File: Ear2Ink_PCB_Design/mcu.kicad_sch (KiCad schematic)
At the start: 11 parts, among them U1 STM32F411RETx

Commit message: added some stuff
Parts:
- added C14: 0.1uF, symbol Device:C
- added C15: 200pF, symbol Device:C
- added J1: Conn_02x16_Top_Bottom, symbol Connector_Generic:Conn_02x16_Top_Bottom
- added MK1: SPH0645LM4H, Sensor_Audio:Knowles_SPH0645LM4H-6_3.5x2.65mm, symbol Sensor_Audio:SPH0645LM4H
- added R3: R_US, symbol Device:R_US
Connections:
- net +3.3V: now also C14.1, C15.1, MK1.2 (SEL), MK1.5 (VDD)
- net GND: now also C14.2, C15.2, MK1.3 (GND)
- net I2S2_SD: now reaches U1.11 (PC3)
- net I2S2_SD: now also R3.1
- net I2S2_MCK: now reaches U1.22 (PA6)
- net I2S2_CK: now reaches U1.29 (PB10)
- net I2S2_CK: now also MK1.4 (BCLK)
- net I2S2_WS: now reaches U1.33 (PB12)
- net I2S2_WS: now also MK1.1 (WS)
- new net: MK1.6 (DATA), R3.2
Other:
- note added: "Note: add or remove these based on trace length"

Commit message: added osc
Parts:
- added C18: 0.1uF, symbol Device:C
- added Y1: MAX7375AXR805, Package_TO_SOT_SMD:SOT-323_SC-70, symbol Oscillator:MAX7375AXR805
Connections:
- net +3.3V: now also J1.18 (Pin_18), J1.2 (Pin_2), C18.1, Y1.1 (V+)
- net GND: now also J1.1 (Pin_1), J1.17 (Pin_17), C18.2, Y1.3 (GND)
- new net RCC_OSC_IN: Y1.2 (CLOCK)

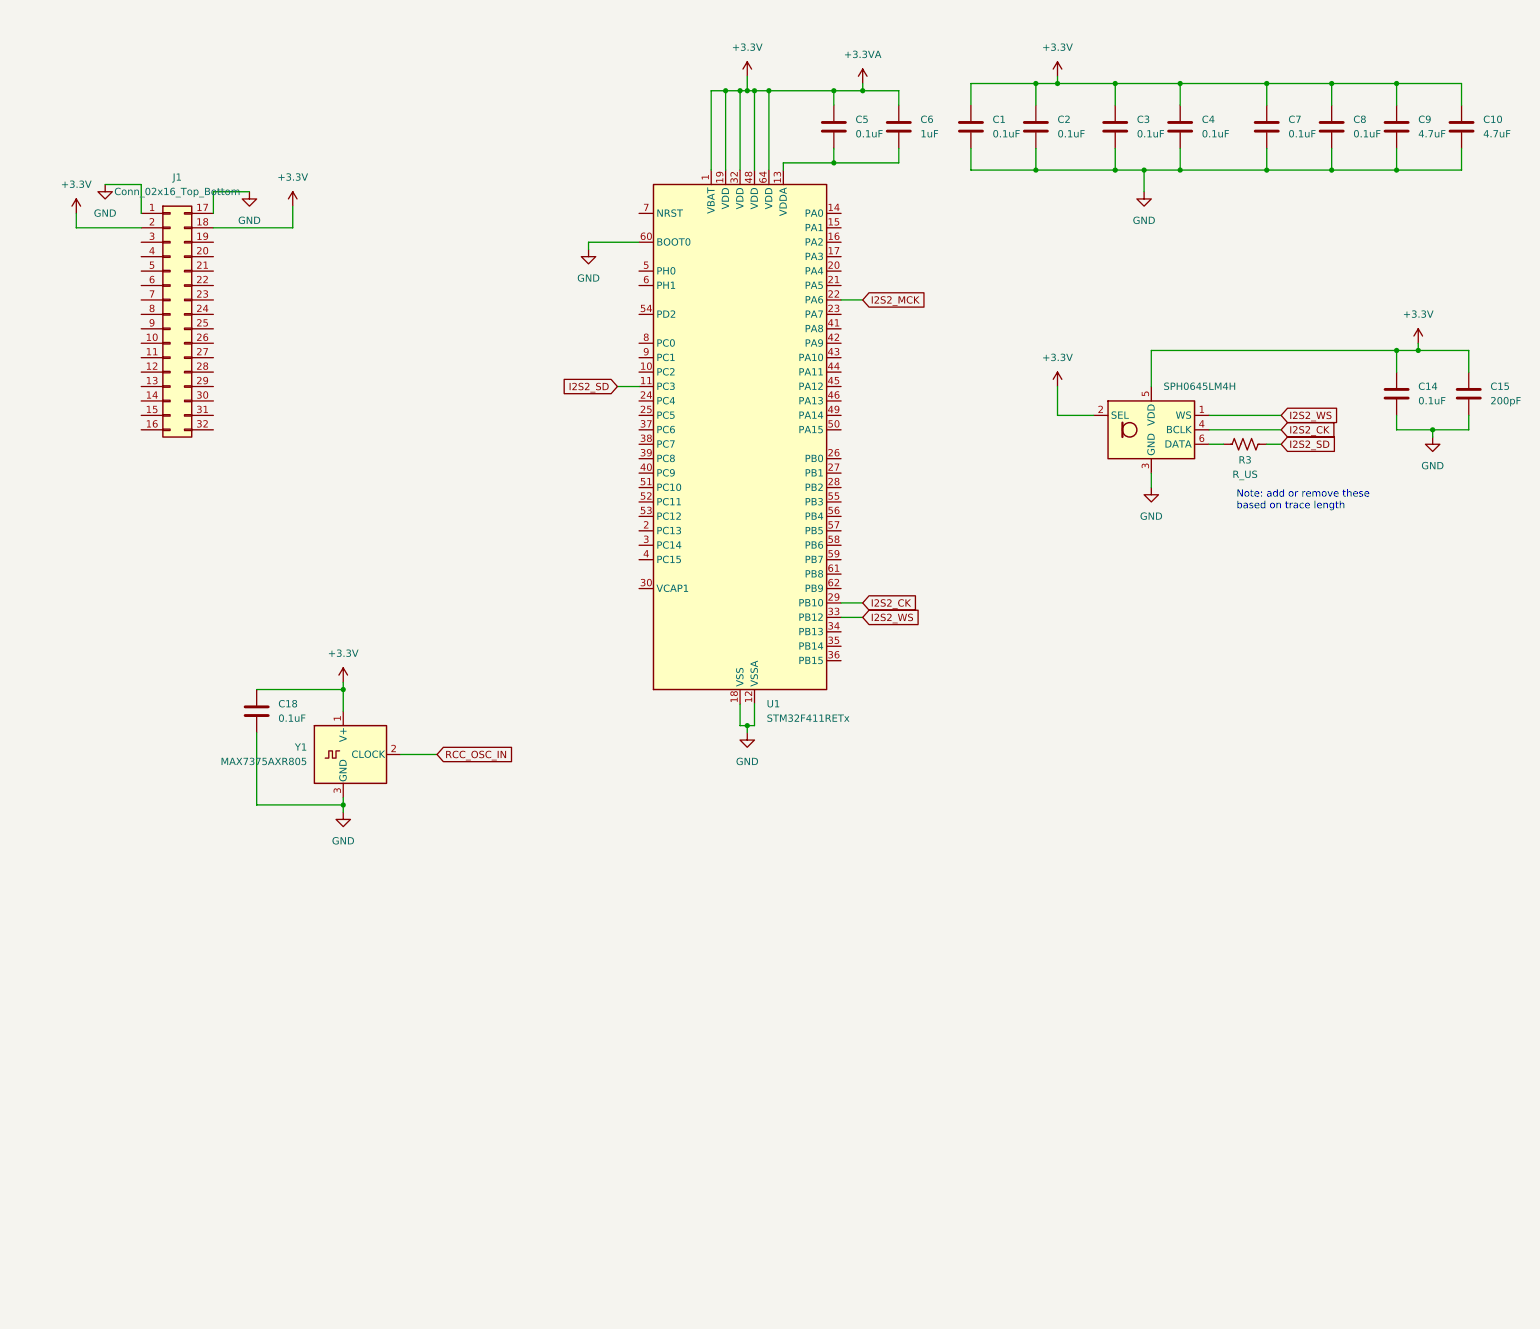
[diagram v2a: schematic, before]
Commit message: wired LCD and keypad
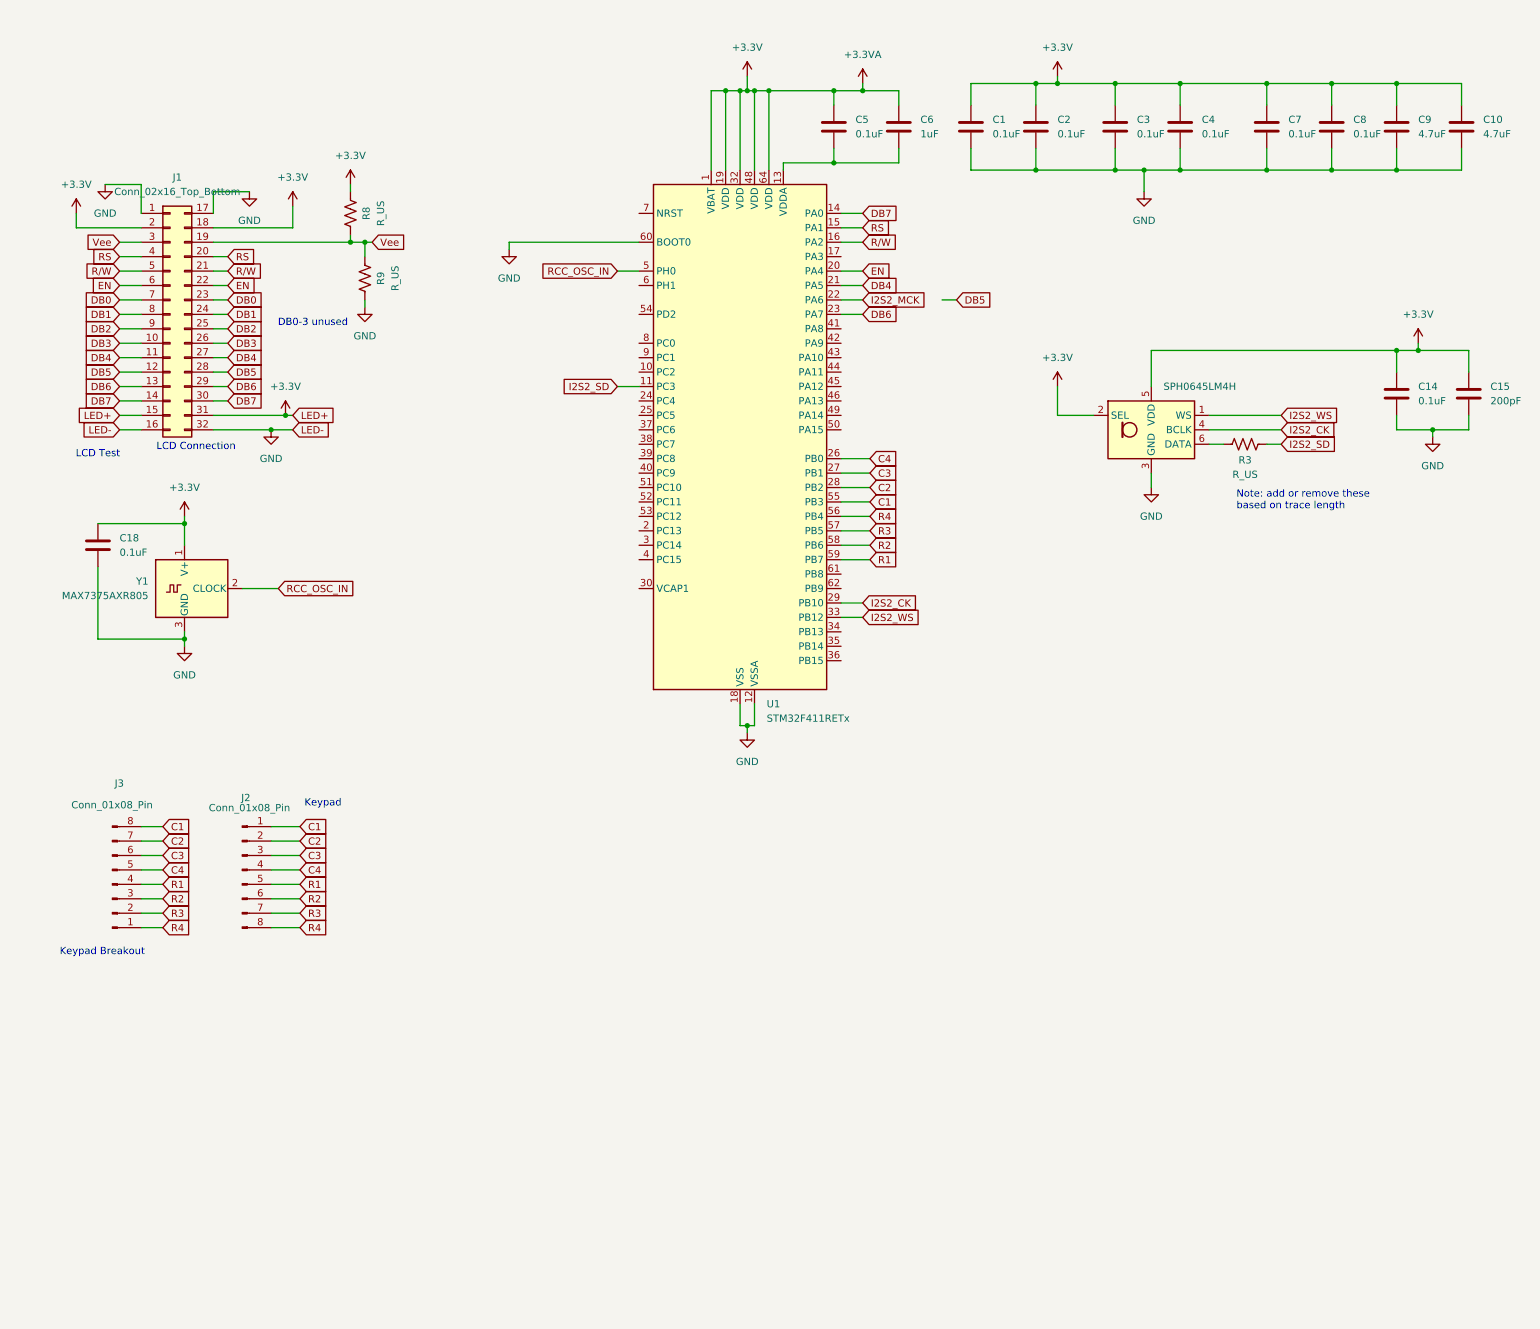
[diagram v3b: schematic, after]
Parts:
- added J2, J3: Conn_01x08_Pin, symbol Connector:Conn_01x08_Pin
- added R8, R9: R_US, symbol Device:R_US
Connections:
- net +3.3V: now also J1.15 (Pin_15), J1.31 (Pin_31), R8.1
- net GND: now also J1.16 (Pin_16), J1.32 (Pin_32), R9.2
- net RCC_OSC_IN: now also U1.5 (PH0)
- net DB7: now reaches U1.14 (PA0)
- net DB7: now also J1.14 (Pin_14), J1.30 (Pin_30)
- net RS: now reaches U1.15 (PA1)
- net RS: now also J1.20 (Pin_20), J1.4 (Pin_4)
- net R/W: now reaches U1.16 (PA2)
- net R/W: now also J1.21 (Pin_21), J1.5 (Pin_5)
- net EN: now reaches U1.20 (PA4)
- net EN: now also J1.22 (Pin_22), J1.6 (Pin_6)
- net DB4: now reaches U1.21 (PA5)
- net DB4: now also J1.11 (Pin_11), J1.27 (Pin_27)
- net DB6: now reaches U1.23 (PA7)
- net DB6: now also J1.13 (Pin_13), J1.29 (Pin_29)
- net C4: now reaches U1.26 (PB0)
- net C4: now also J2.4 (Pin_4), J3.5 (Pin_5)
- net C3: now reaches U1.27 (PB1)
- net C3: now also J2.3 (Pin_3), J3.6 (Pin_6)
- net C2: now reaches U1.28 (PB2)
- net C2: now also J2.2 (Pin_2), J3.7 (Pin_7)
- net C1: now reaches U1.55 (PB3)
- net C1: now also J2.1 (Pin_1), J3.8 (Pin_8)
- net R4: now reaches U1.56 (PB4)
- net R4: now also J2.8 (Pin_8), J3.1 (Pin_1)
- net R3: now reaches U1.57 (PB5)
- net R3: now also J2.7 (Pin_7), J3.2 (Pin_2)
- net R2: now reaches U1.58 (PB6)
- net R2: now also J2.6 (Pin_6), J3.3 (Pin_3)
- net R1: now reaches U1.59 (PB7)
- net R1: now also J2.5 (Pin_5), J3.4 (Pin_4)
- net DB3: now reaches J1.10 (Pin_10)
- net DB3: now also J1.26 (Pin_26)
- net DB5: now reaches J1.12 (Pin_12)
- net DB5: now also J1.28 (Pin_28)
- net Vee: now reaches J1.19 (Pin_19)
- net Vee: now also J1.3 (Pin_3), R8.2, R9.1
- net DB0: now reaches J1.23 (Pin_23)
- net DB0: now also J1.7 (Pin_7)
- net DB1: now reaches J1.24 (Pin_24)
- net DB1: now also J1.8 (Pin_8)
- net DB2: now reaches J1.25 (Pin_25)
- net DB2: now also J1.9 (Pin_9)
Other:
- note added: "DB0-3 unused"
- note added: "Keypad"
- note added: "Keypad Breakout"
- note added: "LCD Connection"
- note added: "LCD Test"
- moved on the sheet: C18, Y1

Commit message: everything except voltage monitor on schematic
no footprints assigned yet
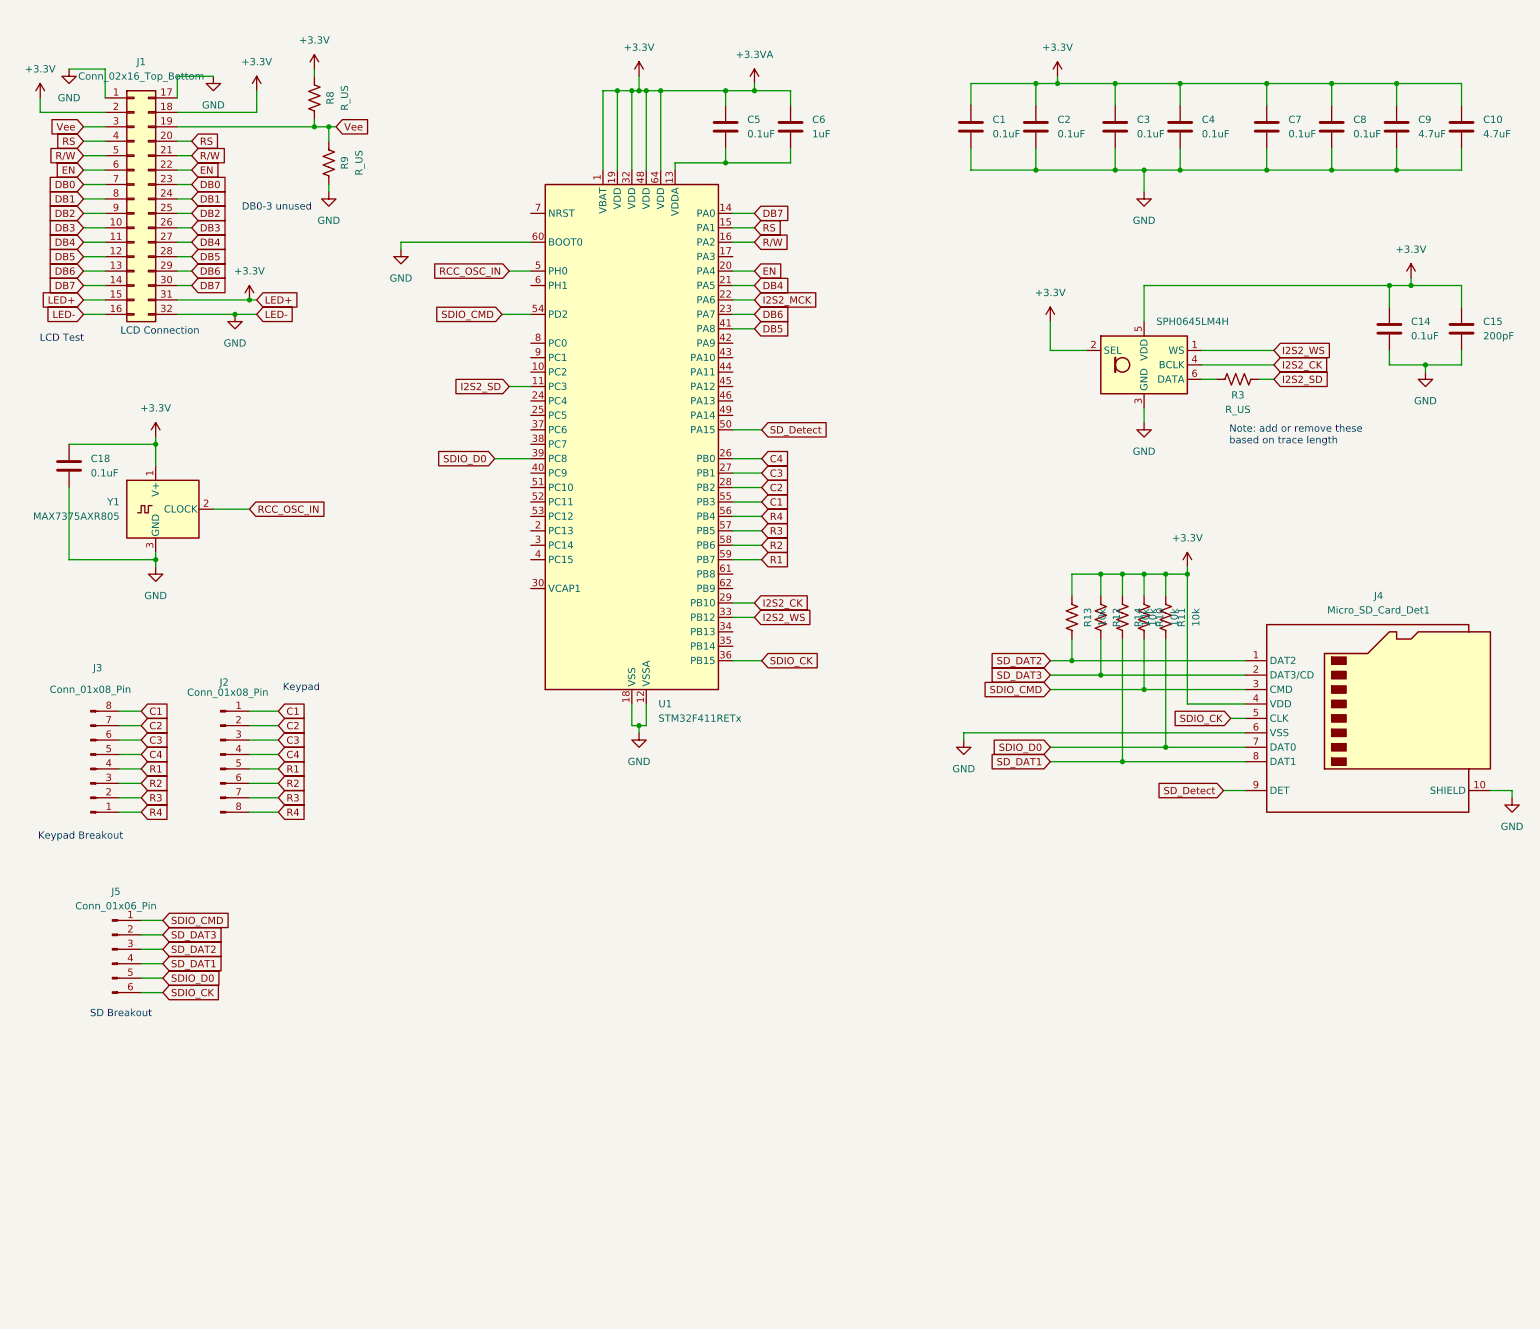
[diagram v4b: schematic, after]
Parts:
- added J4: Micro_SD_Card_Det1, symbol Connector:Micro_SD_Card_Det1
- added J5: Conn_01x06_Pin, symbol Connector:Conn_01x06_Pin
- added R10, R11, R12, R13, R14: 10k, symbol Device:R_US
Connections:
- net +3.3V: now also J4.4 (VDD), R10.1, R11.1, R12.1, R13.1, R14.1
- net DB5: now also U1.41 (PA8)
- net GND: now also J4.10 (SHIELD), J4.6 (VSS)
- net SDIO_CK: now reaches U1.36 (PB15)
- net SDIO_CK: now also J4.5 (CLK), J5.6 (Pin_6)
- net SDIO_D0: now reaches U1.39 (PC8)
- net SDIO_D0: now also J4.7 (DAT0), J5.5 (Pin_5), R11.2
- net SD_Detect: now reaches U1.50 (PA15)
- net SD_Detect: now also J4.9 (DET)
- net SDIO_CMD: now reaches U1.54 (PD2)
- net SDIO_CMD: now also J4.3 (CMD), J5.1 (Pin_1), R10.2
- new net SD_DAT1: J4.8 (DAT1), J5.4 (Pin_4), R14.2
- new net SD_DAT2: J4.1 (DAT2), J5.3 (Pin_3), R13.2
- new net SD_DAT3: J4.2 (DAT3/CD), J5.2 (Pin_2), R12.2
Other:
- note added: "SD Breakout"
- moved on the sheet: C14, C15, C18, C5, C6, J1, J2, J3, R3, R8, R9, U1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

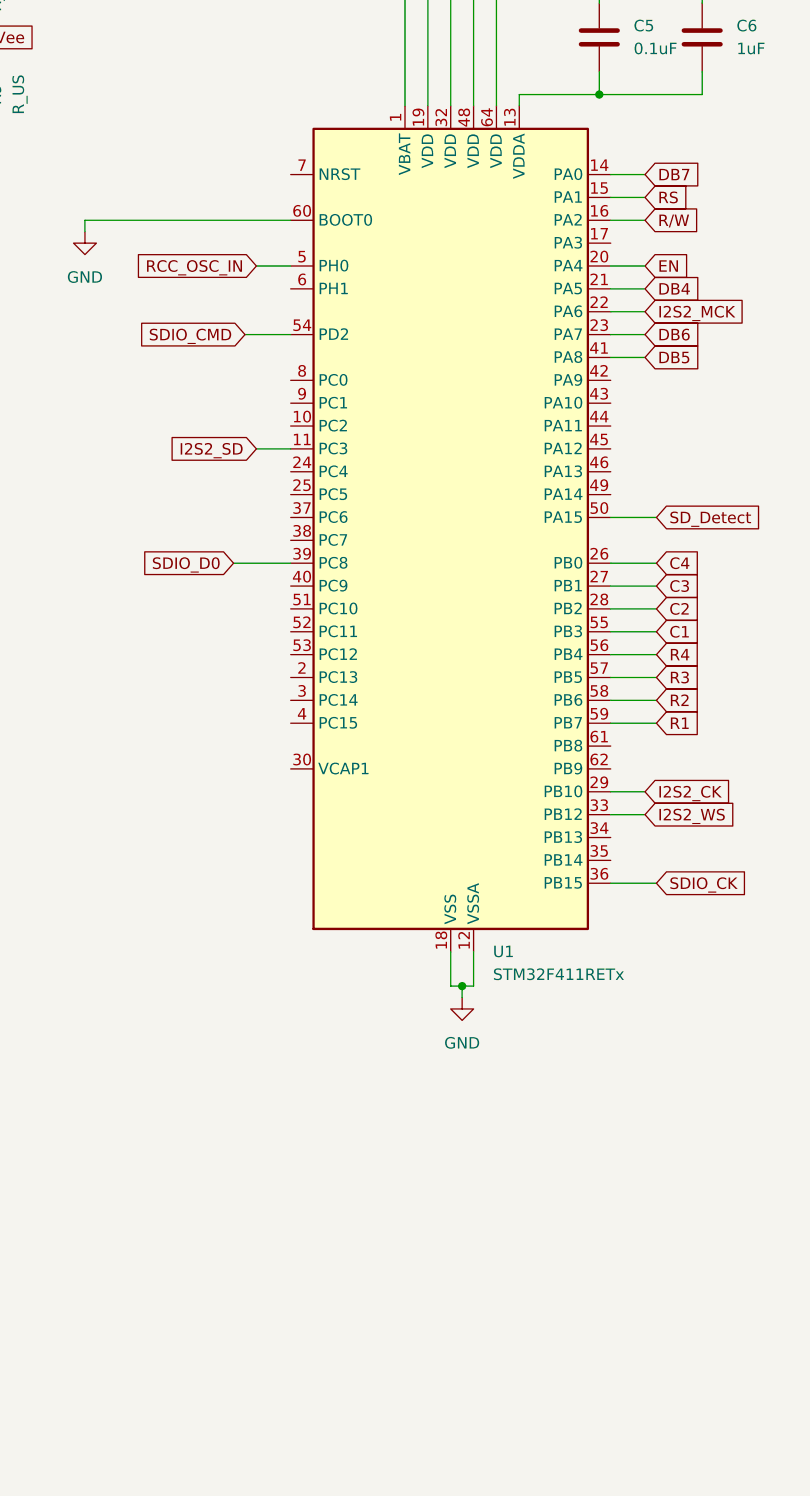
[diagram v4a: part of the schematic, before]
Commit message: started assigning footprints
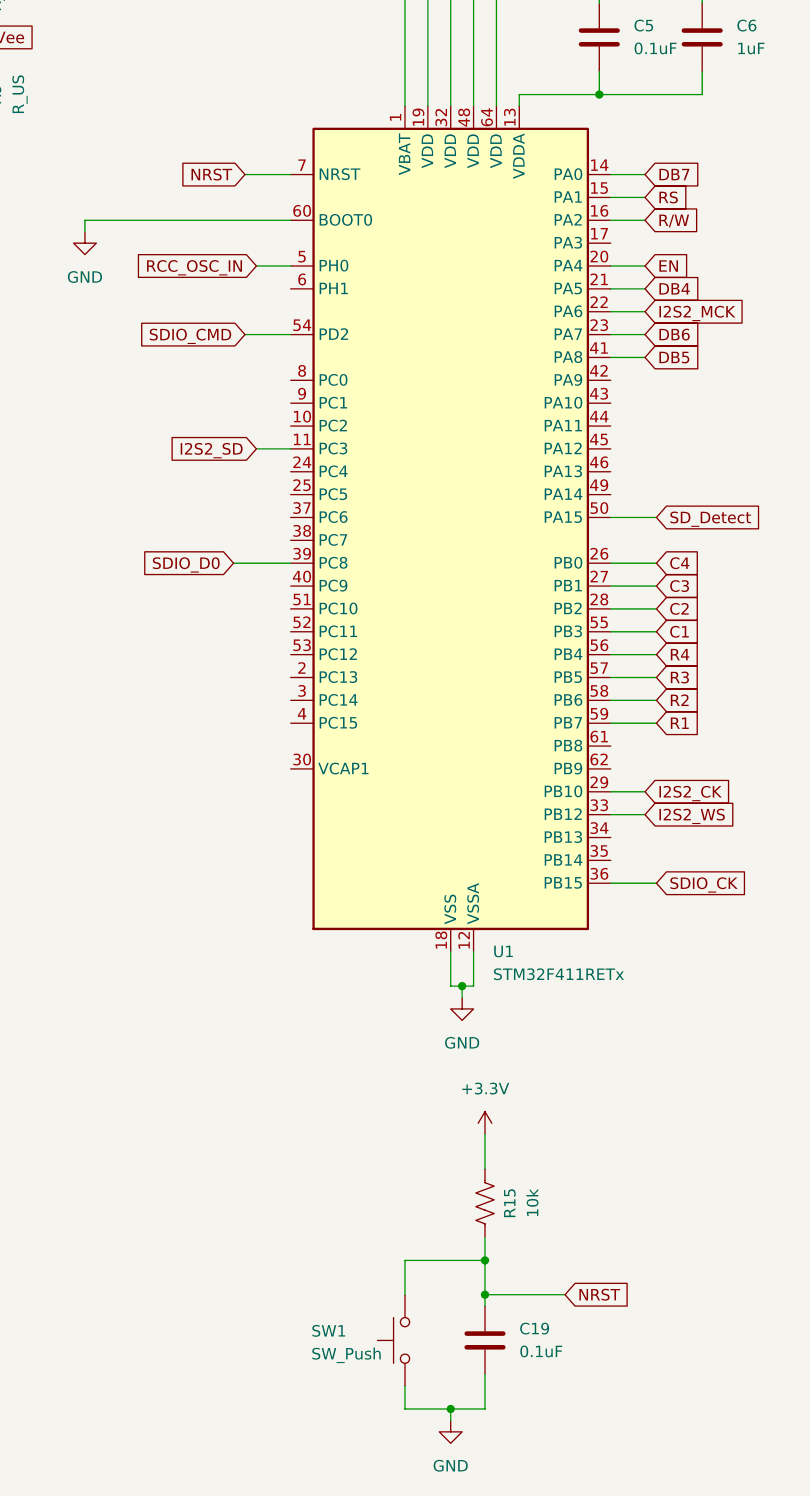
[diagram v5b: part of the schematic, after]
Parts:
- added C19: 0.1uF, symbol Device:C
- added R15: 10k, Capacitor_SMD:C_0603_1608Metric_Pad1.08x0.95mm_HandSolder, symbol Device:R_US
- added SW1: SW_Push, symbol Switch:SW_Push
- R10, R11, R12, R13, R14, R3, R8, R9: footprint (none) -> Capacitor_SMD:C_0603_1608Metric_Pad1.08x0.95mm_HandSolder
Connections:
- net +3.3V: now also R15.1
- net GND: now also C19.2, SW1.1
- net NRST: now reaches U1.7 (NRST)
- net NRST: now also C19.1, R15.2, SW1.2
